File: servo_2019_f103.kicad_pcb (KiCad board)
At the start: 2 copper layers, 45.1 x 86.4 mm, 22 parts, among them J1 Conn_01x20_Female, J3 Alim logique, J4 Conn_01x20_Female, Q1 PMF370XN, Q2 2N7000, Q4 PMF370XN, Q5 2N7000, U1 TC1262-33, U2 w5500, U3 servo_connector

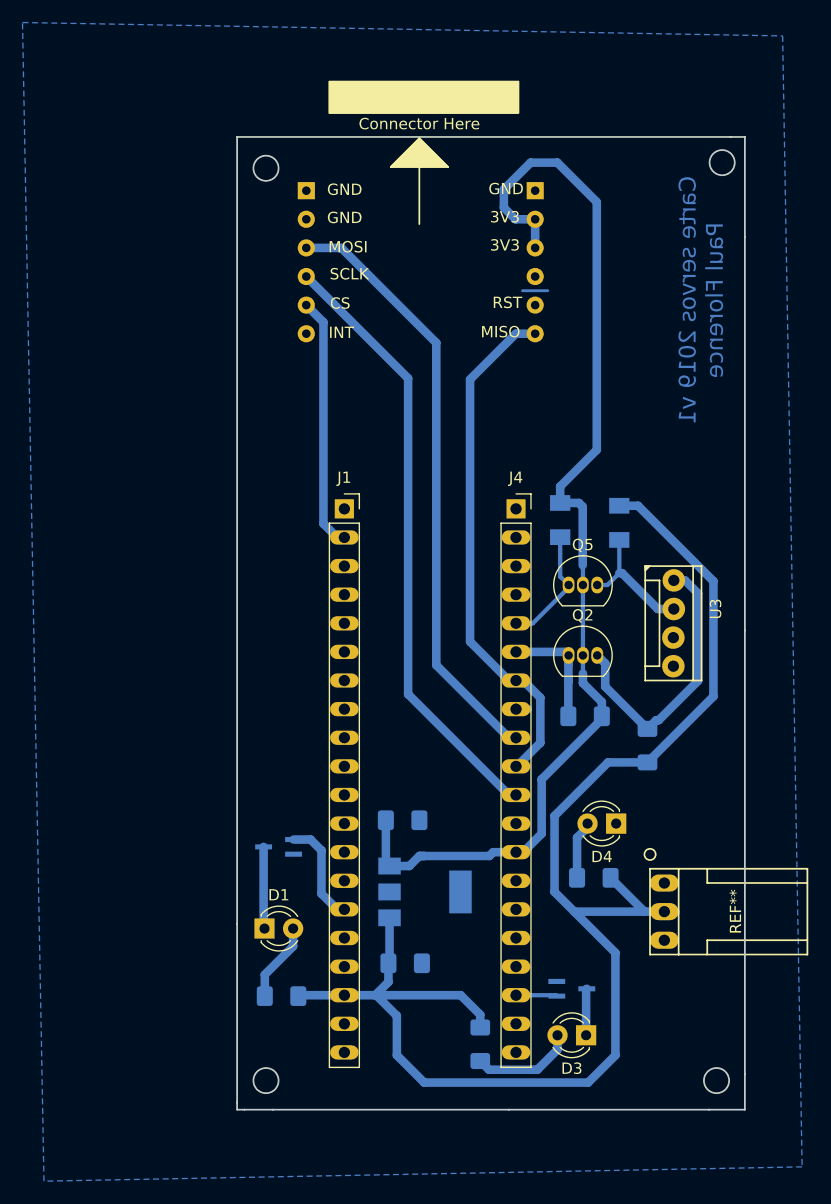
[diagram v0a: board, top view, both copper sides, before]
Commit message: Use bss138 Update connectors Add decoupling capacitor
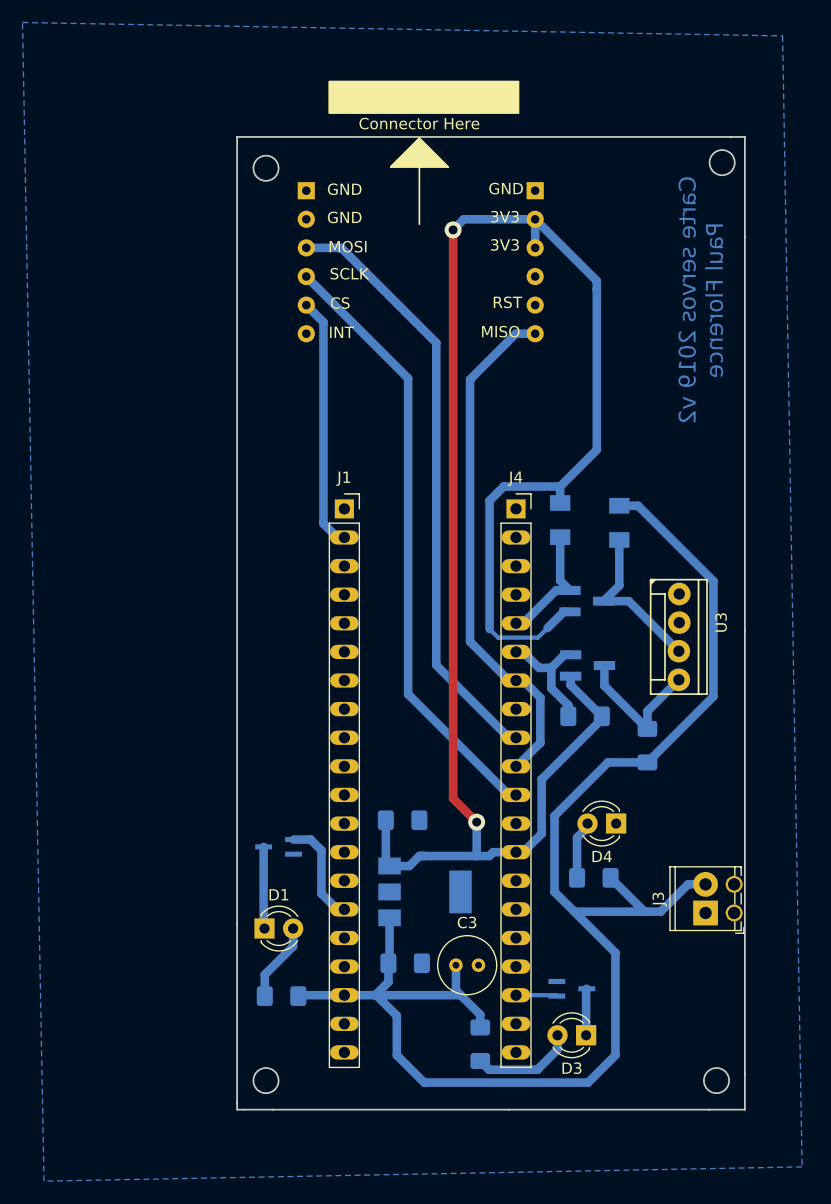
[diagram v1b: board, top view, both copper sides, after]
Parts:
- added C3: 100uF, Capacitor_THT:C_Radial_D5.0mm_H7.0mm_P2.00mm, F.Cu at (126.7, 119.3)
- J3: footprint @Robot:HE14-3_horizontal -> @Robot:TerminalBlock_Phoenix_MPT-0,5-2-2.54_1x02_P2.54mm_Horizontal
- Q2, Q5: value 2N7000 -> BSS138; footprint Package_TO_SOT_THT:TO-92_Inline -> Package_TO_SOT_SMD:SOT-23_Handsoldering; moved to B.Cu
- moved Q5 2.16 mm to (138.4, 86.9)
- moved Q2 1.90 mm to (138.4, 92.6)
- moved U3 1.30 mm to (147.3, 88.8)
- moved J3 0.19 mm to (148.9, 114.6), turned to 90 degrees
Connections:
- Q2 pad 1: /3.3V_logic_tx -> +3V3
- Q2 pad 2: +3V3 -> /3.3V_logic_tx
- Q5 pad 1: /3.3V_logic_rx -> +3V3
- Q5 pad 2: +3V3 -> /3.3V_logic_rx
- U3 pad 1: /5V_logic_tx -> Net-(U3-Pad1)
- U3 pad 2: /5V_logic_rx -> Net-(U3-Pad2)
- U3 pad 3: Net-(U3-Pad3) -> /5V_logic_rx
- U3 pad 4: Net-(U3-Pad4) -> /5V_logic_tx
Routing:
- net +3V3: track 99.6 -> 158.5 mm, vias 0 -> 2
- net /5V_logic_tx: track 25.0 -> 12.7 mm
- net +5V: track 131.2 -> 137.4 mm
- net /5V_logic_rx: track 11.7 -> 14.5 mm
- net GND: track 2.25 -> 0.00 mm
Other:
- board text added: "Carte servos 2019 v2 Paul Florence"
- board text removed: "Carte servos 2019 v1 Paul Florence"
